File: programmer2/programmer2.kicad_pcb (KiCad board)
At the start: 2 copper layers, 63 x 30 mm, 61 parts, among them J1 USB_C_Receptacle_USB2.0_14P, U1 FT2232HL, U3 93CxxA, U4 MIC5504-1.8YM5, U8 AMS1117-3.3, Y1 12MHz

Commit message: Finished programmer 2.
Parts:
- added TP7: TestPoint, TestPoint:TestPoint_THTPad_1.0x1.0mm_Drill0.5mm, F.Cu at (53.8, 26.1)
- added TP8: TestPoint, TestPoint:TestPoint_THTPad_1.0x1.0mm_Drill0.5mm, F.Cu at (53.8, 28.1)
- moved TP1 17.6 mm to (55.8, 22.1)
- moved TP2 17.6 mm to (53.8, 22.1)
- moved TP3 15.5 mm to (53.8, 24.1)
- moved R10 3.93 mm to (58.5, 22.2)
- moved C28 1.84 mm to (51.9, 26.6)
- moved D3 1.70 mm to (49.1, 26.2)
- moved C25 0.80 mm to (51.0, 29.4)
- moved C24 0.70 mm to (62.4, 22.2)
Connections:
- TP1 pad 1: Net-(U1-ACBUS5) -> Net-(TP1-Pad1)
- TP2 pad 1: Net-(U1-ACBUS6) -> Net-(TP2-Pad1)
- TP3 pad 1: Net-(U1-ACBUS7) -> Net-(TP3-Pad1)
- U1 pad 29: unconnected-(U1-ACBUS3-Pad29) -> /FT_ACBUS3
- U1 pad 30: unconnected-(U1-ACBUS4-Pad30) -> /FT_ACBUS4
- U1 pad 32: Net-(U1-ACBUS5) -> /FT_ACBUS5
- U1 pad 33: Net-(U1-ACBUS6) -> /FT_ACBUS6
- U1 pad 34: Net-(U1-ACBUS7) -> /FT_ACBUS7
- U_EPLD1 pad 18: unconnected-(U_EPLD1-I/O-Pad18) -> /FT_ACBUS7
- U_EPLD1 pad 19: /FT_RECONFIG_N -> /FT_ACBUS6
- U_EPLD1 pad 20: /FT_JTAG_SEL_N -> /FT_ACBUS5
- U_EPLD1 pad 21: /FT_JTAG_TMS -> /FT_ACBUS4
- U_EPLD1 pad 22: /FT_JTAG_TDO -> /FT_ACBUS3
- U_EPLD1 pad 24: /FT_JTAG_TDI -> /FT_RECONFIG_N
- U_EPLD1 pad 25: unconnected-(U_EPLD1-I/O-Pad25) -> /FT_JTAG_SEL_N
- U_EPLD1 pad 26: unconnected-(U_EPLD1-I/O-Pad26) -> /FT_JTAG_TMS
- U_EPLD1 pad 27: unconnected-(U_EPLD1-I/O-Pad27) -> /FT_JTAG_TDO
- U_EPLD1 pad 28: unconnected-(U_EPLD1-I/O-Pad28) -> /FT_JTAG_TDI
- U_EPLD1 pad 29: /FT_JTAG_TCK -> /JTAG_LED
- U_EPLD1 pad 30: /JTAG_LED -> /FT_JTAG_TCK
- U_EPLD1 pad 34: /SER_TXD -> Net-(TP1-Pad1)
- U_EPLD1 pad 35: /SER_RXD -> Net-(TP2-Pad1)
- U_EPLD1 pad 36: unconnected-(U_EPLD1-I/O-Pad36) -> Net-(TP3-Pad1)
- U_EPLD1 pad 37: /IO4B -> Net-(TP7-Pad1)
- U_EPLD1 pad 38: /IO4A -> Net-(TP8-Pad1)
- U_EPLD1 pad 40: unconnected-(U_EPLD1-I/O-Pad40) -> /SER_TXD
- U_EPLD1 pad 42: unconnected-(U_EPLD1-I/O-Pad42) -> /SER_RXD
- U_EPLD1 pad 43: unconnected-(U_EPLD1-I/O-Pad43) -> /IO4B
- U_EPLD1 pad 44: unconnected-(U_EPLD1-I/O-Pad44) -> /IO4A
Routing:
- net /FT_ACBUS3: track 0.00 -> 16.4 mm
- net /FT_ACBUS4: track 0.00 -> 15.1 mm
- net /FT_ACBUS5: track 0.00 -> 13.7 mm
- net /FT_ACBUS7: track 0.00 -> 11.5 mm
- net /FT_ACBUS6: track 0.00 -> 11.3 mm
- net VIO: track 22.2 -> 29.4 mm, vias 5 -> 7
- net Net-(TP2-Pad1): track 0.00 -> 6.22 mm
- net Net-(U1-ACBUS7): track 6.21 -> 0.00 mm
- net Net-(TP1-Pad1): track 0.00 -> 5.73 mm
- net Net-(D4-A): track 2.47 -> 7.80 mm
- net VCC: track 74.3 -> 79.4 mm, vias 15 -> 18
- net Net-(TP3-Pad1): track 0.00 -> 4.72 mm
- net Net-(U1-ACBUS6): track 4.60 -> 0.00 mm
- net /FT_JTAG_TMS: track 22.8 -> 27.3 mm
- net /FT_JTAG_TDO: track 23.5 -> 27.8 mm
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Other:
- board text removed: "J_SEL"
- board text removed: "RCFG"
- board text removed: "RXD"
- board text removed: "TARGET"
- board text removed: "TXD"
- board text removed: "USB"

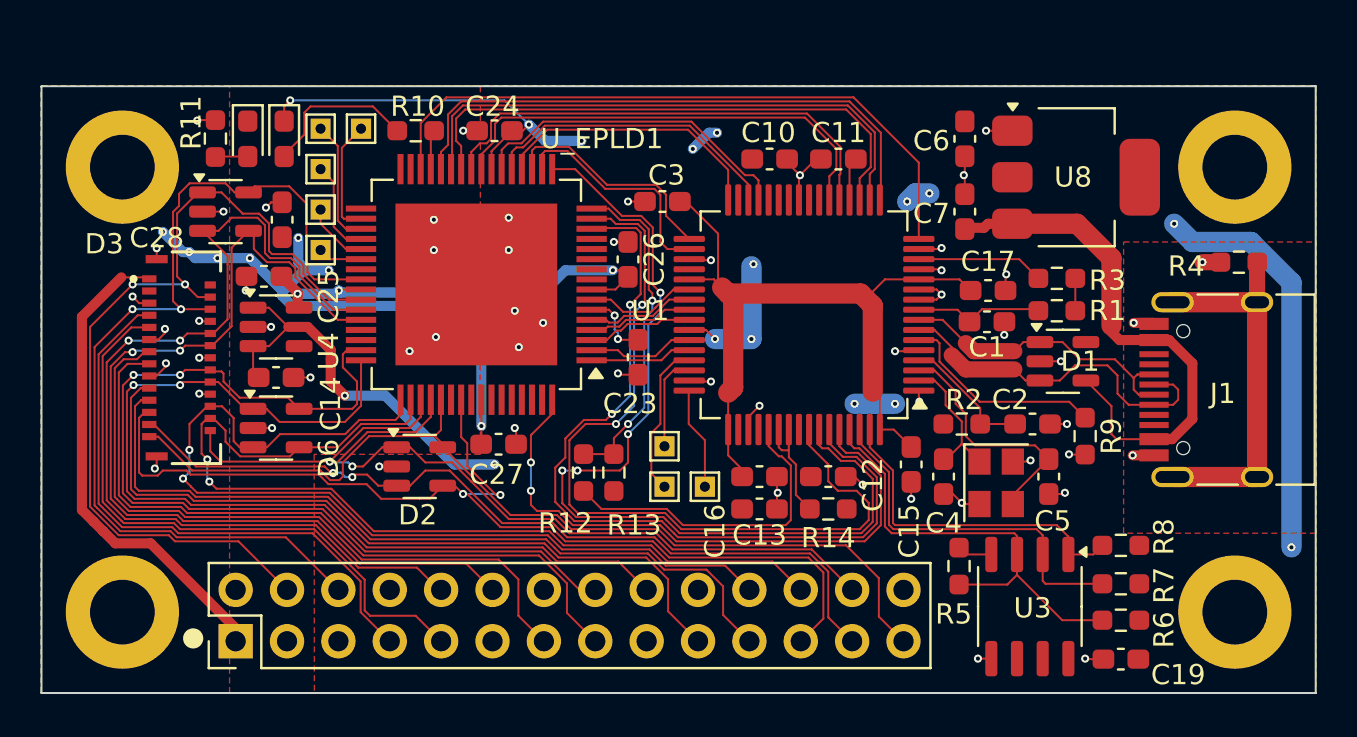
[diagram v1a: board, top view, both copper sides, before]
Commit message: Beautified schematic and PCB for programmer 2.
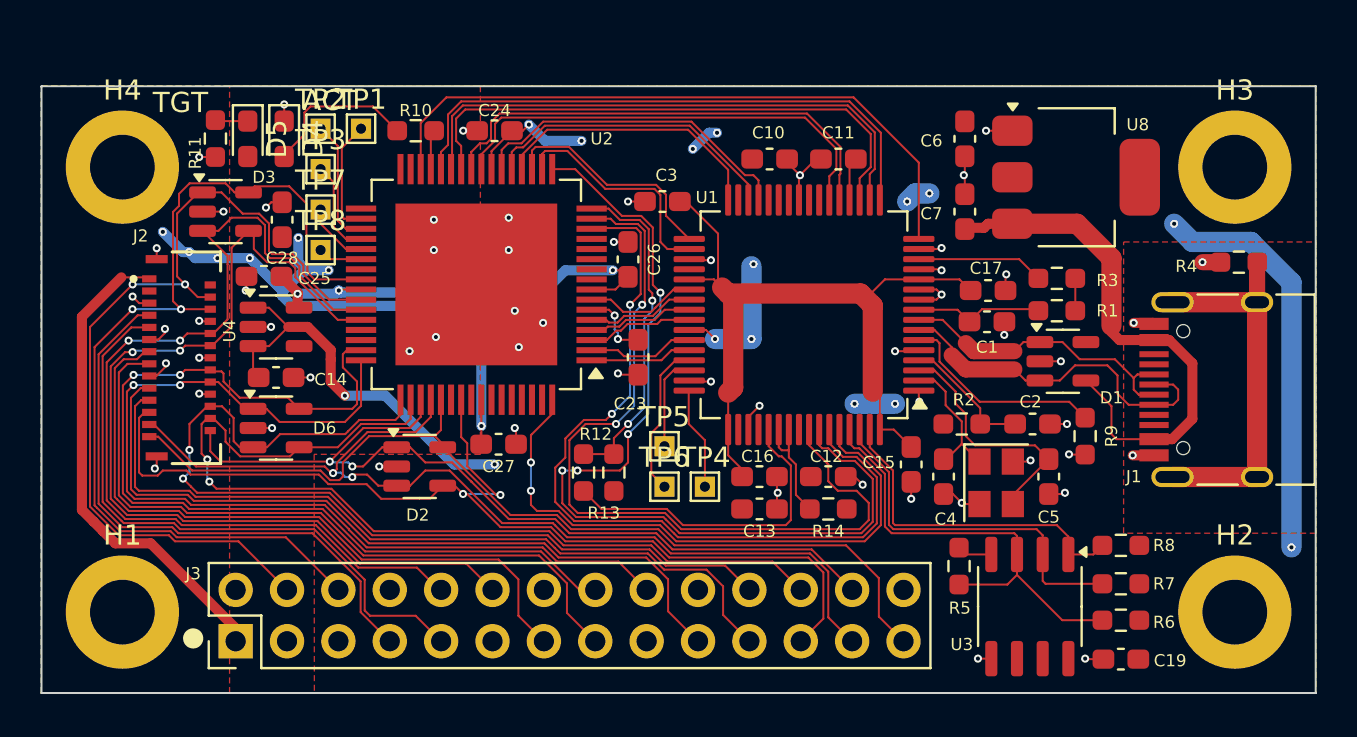
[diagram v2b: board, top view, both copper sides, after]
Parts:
- D4, D5: footprint LED_SMD:LED_0603_1608Metric_Pad1.05x0.95mm_HandSolder -> unic:LED_0603_1608Metric_Pad1.05x0.95mm_HandSolder
- H1, H2, H3, H4: footprint MountingHole:MountingHole_3.2mm_M3_DIN965_Pad -> unic:MountingHole_3.2mm_M3_DIN965_Pad
- TP1, TP2, TP3, TP4, TP5, TP6, TP7, TP8: footprint TestPoint:TestPoint_THTPad_1.0x1.0mm_Drill0.5mm -> unic:TestPoint_THTPad_1.0x1.0mm_Drill0.5mm
- turned R10 to 180 degrees
- turned R11 to -90 degrees
- renumbered J_EXT1 to J2, J_EXT2 to J3, U_EPLD1 to U2
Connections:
- net Net-(U1-VPHY) renamed /VPHY
- net Net-(U1-VPLL) renamed /VPLL
- net VCORE renamed V_FCORE
- D4 pad 1: VCC -> GND
- D5 pad 1: VIO -> Net-(D5-K)
- D5 pad 2: Net-(D5-A) -> VIO
- R10 pad 1: Net-(D4-A) -> /JTAG_LED
- R10 pad 2: /JTAG_LED -> Net-(D4-A)
- R11 pad 1: Net-(D5-A) -> Net-(D5-K)
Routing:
- net VCC: track 79.4 -> 66.0 mm, vias 18 -> 17
- net Net-(D5-K): track 0.00 -> 1.72 mm
- net Net-(D5-A): track 1.61 -> 0.00 mm
- net GND: track 50.2 -> 51.1 mm, vias 57 -> 58
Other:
- board text added: "ACT"
- board text added: "TGT"

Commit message: Updated programmer schematic and PCBs.
All known changes are incorporated.

p.s.: I decided to stick with this rather sketchy LDO.
The reason for this is that it's heatsink tab is connected
to VCC, which happens to be the fill on the top layer
so a GND-connected alternative would be less well cooled.
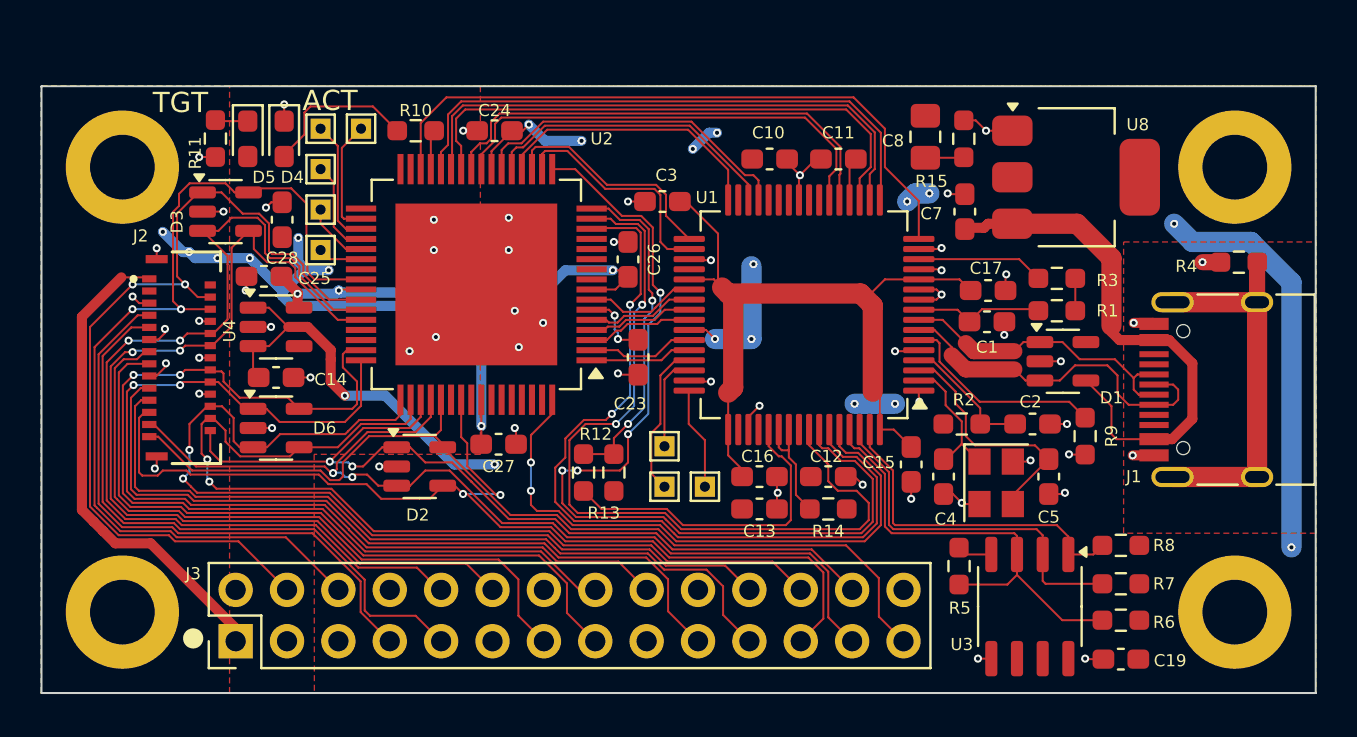
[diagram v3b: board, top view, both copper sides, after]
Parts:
- removed C6: 3.3u, Capacitor_SMD:C_0603_1608Metric_Pad1.08x0.95mm_HandSolder
- added C8: 22u, Capacitor_SMD:C_0805_2012Metric_Pad1.18x1.45mm_HandSolder, F.Cu at (83.7, 22.5)
- added R15: 2.2, Resistor_SMD:R_0603_1608Metric_Pad0.98x0.95mm_HandSolder, F.Cu at (85.6, 22.6)
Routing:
- net Net-(C8-Pad2): track 0.00 -> 1.91 mm
